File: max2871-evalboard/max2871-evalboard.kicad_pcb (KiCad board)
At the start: 4 copper layers, 50 x 80 mm, 117 parts, among them J101 USB_B_Mini, J102 Conn_02x05, J103 Conn_02x06_Odd_Even, J104 Conn_Coaxial, J105 Conn_Coaxial, Q201 2N7002, Q202 2N7002, SW101 XKBS22E05-Z, SW201 SW_Push, SW202 SW_Push, U201 AZ1117-3.3, U202 W25Q128JVS, U203 RP2040, U301 LP5907MFX-3.3, U302 LP5907MFX-3.3, U303 LP5907MFX-1.8, U304 54M_P3225, U305 MAX2871ETJ+, Y201 Crystal

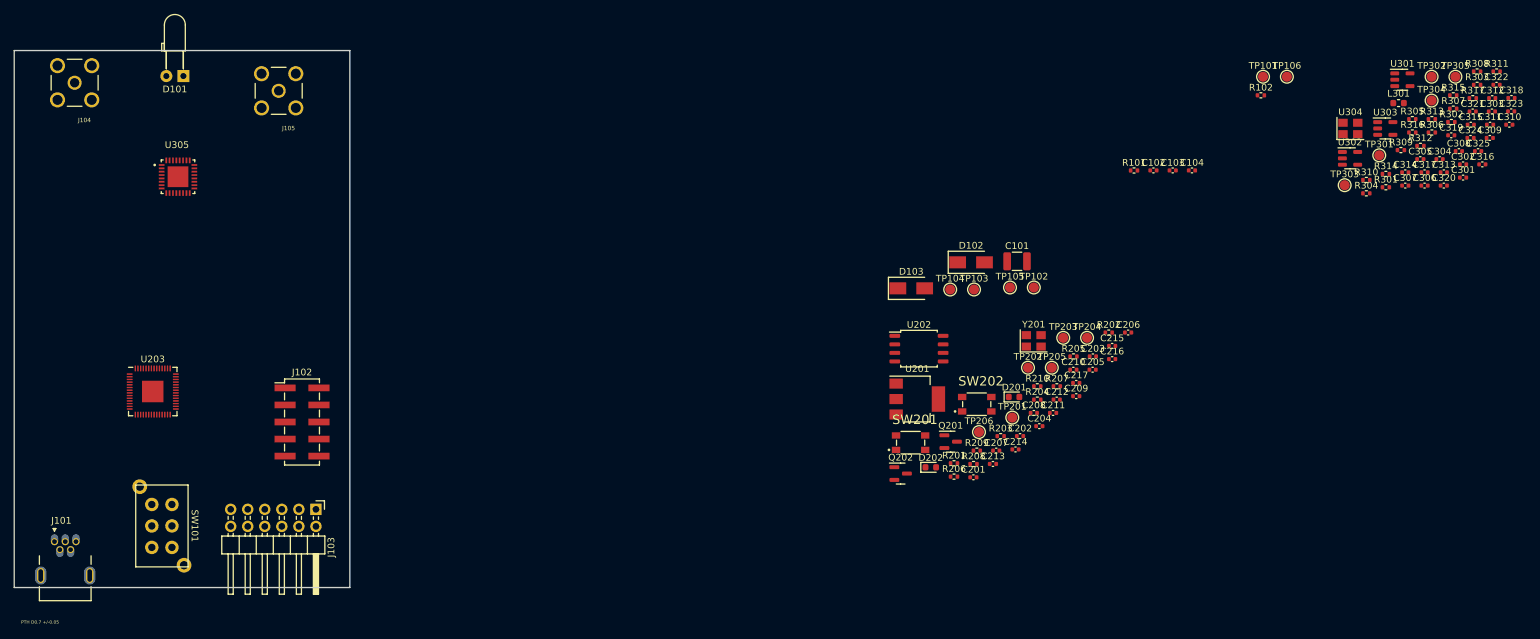
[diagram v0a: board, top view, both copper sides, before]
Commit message: Finished schematics - started PCB design
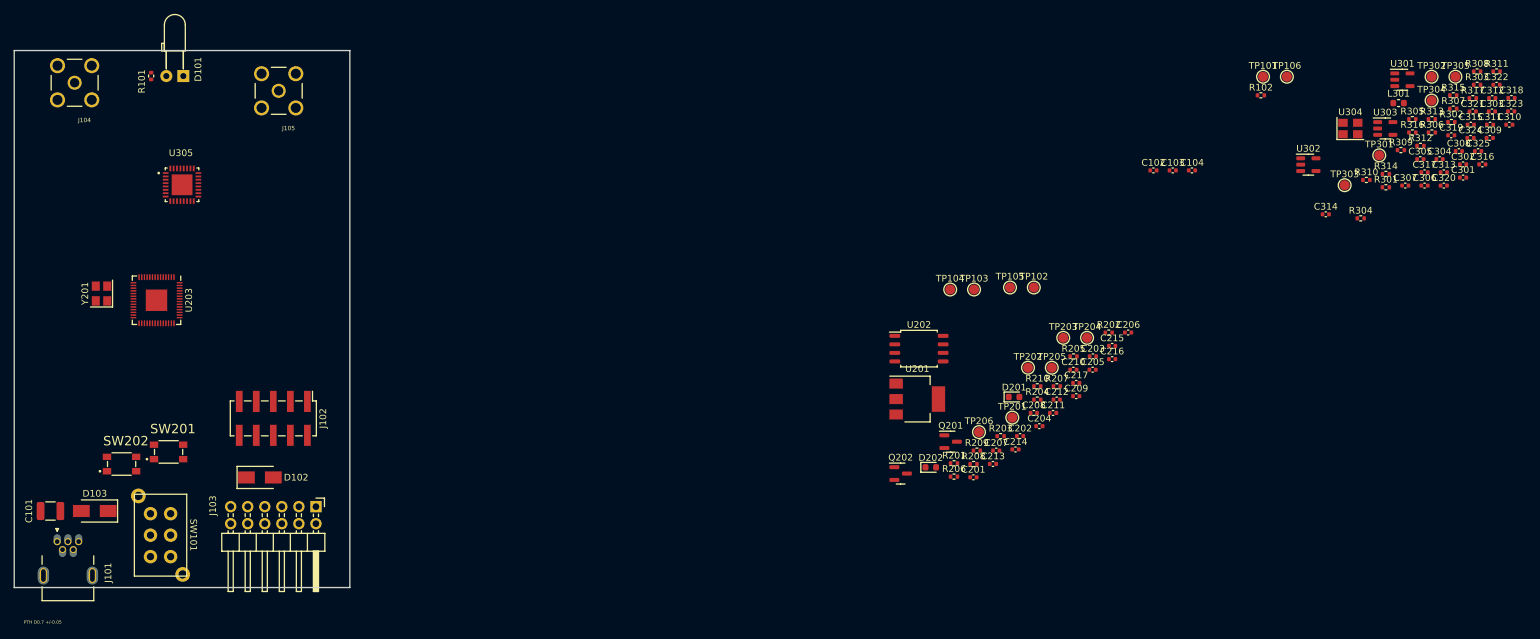
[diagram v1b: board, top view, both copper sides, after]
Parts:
- moved C101 148.7 mm to (55.4, 118.6), turned to 180 degrees
- moved R101 147.1 mm to (70.4, 53.8), turned to -90 degrees
- moved Y201 139.1 mm to (63.0, 86.2), turned to 90 degrees
- moved SW202 127.7 mm to (66.0, 111.6)
- moved D103 126.1 mm to (62.0, 118.6), turned to 180 degrees
- moved D102 110.7 mm to (86.6, 113.6)
- moved SW201 110.6 mm to (73.0, 109.8)
- moved U203 13.6 mm to (71.2, 87.2), turned to -90 degrees
- moved C314 13.4 mm to (245.4, 74.4)
- moved U302 6.28 mm to (242.8, 67.0)
- moved J102 4.31 mm to (88.6, 104.8), turned to -90 degrees
- moved R304 3.82 mm to (250.6, 75.0)
- moved SW101 1.39 mm to (71.8, 122.2)
- moved U305 1.34 mm to (75.0, 70.0)
- moved J101 0.40 mm to (56.4, 123.2)
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
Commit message: PCB placement complete
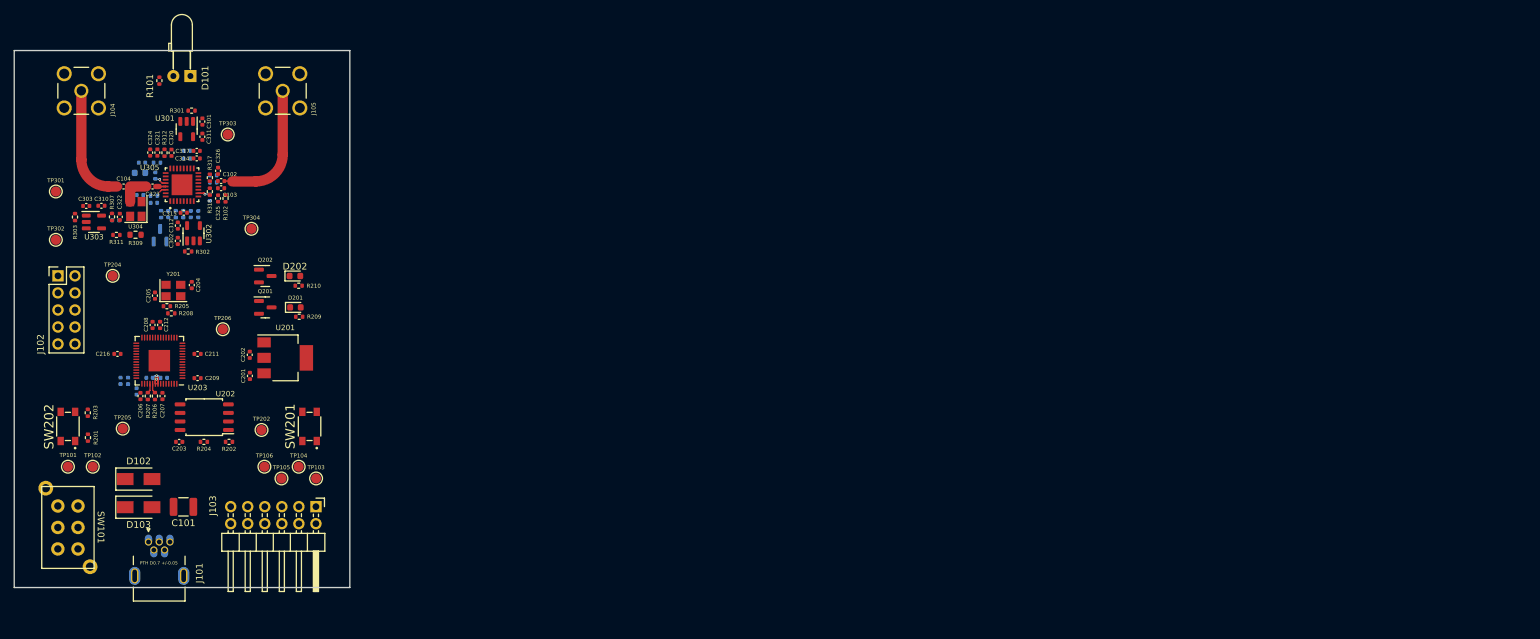
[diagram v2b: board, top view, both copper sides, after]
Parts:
- removed TP201, TP203: , TestPoint:TestPoint_Pad_D1.5mm
- removed the TP304 at (261.2, 57.5)
- added C319: 100pF, Capacitor_SMD:C_0402_1005Metric, B.Cu at (72.9, 74.4)
- added Q301: 2N7002, Package_TO_SOT_SMD:SOT-23, B.Cu at (71.7, 77.5)
- added R310: 1k, Resistor_SMD:R_0402_1005Metric, B.Cu at (71.9, 74.4)
- C210, C213, C214, C215, C217, C304, C305, C306, C307, C308, C309, C313, C316, C318, L301, R304, R305, R306, R308: moved to B.Cu
- J102: footprint Connector_PinHeader_2.54mm:PinHeader_2x05_P2.54mm_Vertical_SMD -> Connector_PinHeader_2.54mm:PinHeader_2x05_P2.54mm_Vertical
- R309: footprint Resistor_SMD:R_0402_1005Metric -> Resistor_SMD:R_0603_1608Metric
- R313: renamed from R312; moved to B.Cu
- R314: renamed from R313; moved to B.Cu
- R315: renamed from R314; moved to B.Cu
- R316: renamed from R315; moved to B.Cu
- moved C310 210.1 mm to (63.0, 73.1), turned to 180 degrees
- moved TP302 209.9 mm to (56.2, 78.2)
- moved C303 209.9 mm to (60.7, 73.2)
- moved R303 209.8 mm to (59.1, 74.8), turned to -90 degrees
- moved R308 204.0 mm to (65.1, 75.3), turned to 180 degrees
- moved C324 202.9 mm to (70.3, 65.2), turned to 90 degrees
- moved C322 202.2 mm to (65.7, 74.8), turned to -90 degrees
- moved C309 200.8 mm to (69.0, 66.7), turned to 180 degrees
- moved C323 200.8 mm to (70.6, 70.3), turned to 180 degrees
- moved R307 200.5 mm to (64.6, 74.8), turned to -90 degrees
- moved R312 198.8 mm to (72.4, 65.2), turned to 90 degrees
- moved C316 198.0 mm to (70.8, 72.7), turned to 180 degrees
- moved TP301 197.2 mm to (56.2, 71.0)
- moved C312 196.7 mm to (74.4, 76.1), turned to -90 degrees
- moved C318 194.5 mm to (79.1, 71.9), turned to -90 degrees
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- renumbered C319 to C320, C320 to C321, C321 to C322, C322 to C323, C323 to C324, C324 to C325, C325 to C326, R310 to R311, R311 to R312, R316 to R317, R317 to R318, TP305 to TP302, TP302 to TP303, TP303 to TP304
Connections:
- J103 pad 8: /CE -> /LE
- TP106 pad 1: /CE -> /LE
- U203 pad 12: /microcontroller/VCO_LE -> unconnected-(U203-Pad12)
- U203 pad 13: unconnected-(U203-Pad13) -> /microcontroller/LED1
- U203 pad 14: unconnected-(U203-Pad14) -> /microcontroller/LED2
- U203 pad 36: /microcontroller/LED1 -> unconnected-(U203-Pad36)
- U203 pad 37: /microcontroller/LED2 -> unconnected-(U203-Pad37)
- U203 pad 7: /microcontroller/VCO_MUX -> /microcontroller/VCO_CE
- U305 pad 3: /microcontroller/VCO_LE -> /LE
- U305 pad 4: /CE -> Net-(C319-Pad1)
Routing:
- net Net-(C102-Pad2): track 0.00 -> 26.8 mm
- net Net-(C104-Pad1): track 0.00 -> 23.0 mm
- net +3V3: track 0.00 -> 7.25 mm, vias 0 -> 2
- net /vco/REF_CLK: track 0.00 -> 5.11 mm
- net /vco/VCC_DIG: track 0.00 -> 2.05 mm, vias 0 -> 1
- net Net-(C323-Pad1): track 0.00 -> 1.98 mm
- net /vco/VCC_PLL: track 0.00 -> 1.78 mm, vias 0 -> 1
- net Net-(R206-Pad2): track 0.00 -> 1.46 mm
- net Net-(R207-Pad2): track 0.00 -> 1.45 mm
- net /MUX: track 0.00 -> 1.02 mm

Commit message: Finish PCB design
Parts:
- moved TP204 11.2 mm to (54.7, 78.5)
- moved TP202 8.16 mm to (80.1, 111.1)
- moved C101 6.90 mm to (68.4, 119.3), turned to 180 degrees
- moved TP302 3.57 mm to (55.5, 74.7)
- moved D103 2.51 mm to (68.5, 115.5)
- moved D102 2.16 mm to (68.5, 111.7)
- moved TP206 1.84 mm to (79.2, 91.3)
- moved TP303 1.63 mm to (80.2, 62.4)
- moved R208 1.03 mm to (74.0, 90.0)
- moved C201 1.01 mm to (85.1, 97.5), turned to 90 degrees
- moved R205 0.86 mm to (73.0, 88.9)
- moved C204 0.86 mm to (76.7, 85.8)
- moved C205 0.86 mm to (71.2, 87.3)
- moved Y201 0.86 mm to (74.0, 86.6)
- moved R302 0.76 mm to (76.7, 79.9)
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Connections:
- J101 pad 6: GND -> (no net)
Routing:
- net +3V3: track 7.25 -> 114.2 mm, vias 2 -> 23
- net /PWR: track 0.00 -> 82.4 mm, vias 0 -> 18
- net /DATA: track 0.00 -> 69.7 mm
- net /MUX: track 1.02 -> 64.4 mm, vias 0 -> 1
- net /SCLK: track 0.00 -> 62.6 mm
- net /microcontroller/VCO_LD: track 0.00 -> 61.0 mm, vias 0 -> 3
- net /EN_TXCO: track 0.00 -> 60.3 mm, vias 0 -> 1
- net /RESET: track 0.00 -> 58.1 mm, vias 0 -> 1
- net /LE: track 0.00 -> 57.3 mm, vias 0 -> 2
- net /microcontroller/VCOOUT_EN: track 0.00 -> 56.6 mm, vias 0 -> 3
- net /TXCO_PWR: track 0.00 -> 54.8 mm, vias 0 -> 1
- net GND: track 0.00 -> 51.9 mm, vias 0 -> 231
- net /SPI_CLK: track 0.00 -> 50.1 mm, vias 0 -> 1
- net /SPI_DATA: track 0.00 -> 47.0 mm, vias 0 -> 1
- net /SPI_MISO: track 0.00 -> 41.2 mm, vias 0 -> 1
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- added copper zone on F.Cu, net +3V3
- added copper zone on In1.Cu, net +3V3
- added copper zone on B.Cu, net /PWR
- added copper zone on F.Cu, net /PWR
- added copper zone on In1.Cu, net /PWR
- added copper zone on B.Cu, net GND
- added copper zone on F.Cu, net GND
- added copper zone on In1.Cu, net GND
- added copper zone on In2.Cu, net GND

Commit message: Finish layout design
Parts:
- removed the C302 at (74.4, 78.4)
- removed the C303 at (60.7, 73.2)
- removed the C310 at (63.0, 73.1)
- removed the C312 at (74.4, 76.1)
- removed the R302 at (76.7, 79.9)
- removed the R303 at (59.1, 74.8)
- removed the R308 at (65.1, 75.3)
- removed the TP302 at (55.5, 74.7)
- removed the U302 at (76.7, 77.2)
- removed the U303 at (61.9, 75.5)
- added C204: 2.2uF, Capacitor_SMD:C_0402_1005Metric, F.Cu at (72.9, 106.6)
- added C304: 100nF, Capacitor_SMD:C_0402_1005Metric, F.Cu at (77.2, 63.0)
- added C305: 100nF, Capacitor_SMD:C_0402_1005Metric, F.Cu at (78.2, 74.7)
- added C315: 100pF, Capacitor_SMD:C_0402_1005Metric, F.Cu at (78.8, 66.3)
- added C316: 100pF, Capacitor_SMD:C_0402_1005Metric, F.Cu at (75.2, 74.0)
- added D201: LED, LED_THT:LED_D3.0mm_Horizontal_O3.81mm_Z2.0mm, F.Cu at (81.5, 53.7)
- added L301: BLM18PG181S, Inductor_SMD:L_0603_1608Metric, F.Cu at (76.6, 61.5)
- added L302: BLM18PG181S, Inductor_SMD:L_0603_1608Metric, F.Cu at (81.5, 75.9)
- added Q201: 2N7002, Package_TO_SOT_SMD:SOT-23, F.Cu at (80.3, 58.2)
- added R101: DNP, Resistor_SMD:R_0402_1005Metric, F.Cu at (68.2, 120.4)
- added R102: 5.1k, Resistor_SMD:R_0402_1005Metric, F.Cu at (75.3, 119.6)
- added R103: DNP, Resistor_SMD:R_0402_1005Metric, F.Cu at (67.1, 120.4)
- added R104: 5.1k, Resistor_SMD:R_0402_1005Metric, F.Cu at (74.1, 119.6)
- added R209: 1k, Resistor_SMD:R_0402_1005Metric, F.Cu at (79.3, 55.6)
- added REF**: MountingHole_2.7mm_M2.5_DIN965, MountingHole:MountingHole_2.7mm_M2.5_DIN965, F.Cu at (96.0, 65.0)
- added REF**: MountingHole_2.7mm_M2.5_DIN965, MountingHole:MountingHole_2.7mm_M2.5_DIN965, F.Cu at (54.0, 110.0)
- added REF**: MountingHole_2.7mm_M2.5_DIN965, MountingHole:MountingHole_2.7mm_M2.5_DIN965, F.Cu at (96.0, 110.0)
- added REF**: MountingHole_2.7mm_M2.5_DIN965, MountingHole:MountingHole_2.7mm_M2.5_DIN965, F.Cu at (54.0, 65.0)
- added REF**: OSHW-Logo2_14.6x12mm_SilkScreen, Symbol:OSHW-Logo2_14.6x12mm_SilkScreen, B.Cu at (64.8, 105.2)
- C101: value 47uF -> 10uF; footprint Capacitor_SMD:C_1210_3225Metric -> Capacitor_SMD:C_0603_1608Metric
- C201: value 1uF -> 10uF; footprint Capacitor_SMD:C_0402_1005Metric -> Capacitor_SMD:C_0603_1608Metric
- C202: value 1uF -> 22uF; footprint Capacitor_SMD:C_0402_1005Metric -> Capacitor_SMD:C_0805_2012Metric
- J101: value USB_B_Mini -> USB_C_Receptacle_USB2.0; footprint 54819-0519:MOLEX_54819-0519 -> USB4105-GF-A:GCT_USB4105-GF-A
- J103: renamed from J102; footprint Connector_PinHeader_2.54mm:PinHeader_2x05_P2.54mm_Vertical -> Connector_PinHeader_1.27mm:PinHeader_2x05_P1.27mm_Vertical
- TP101: renamed from TP103; footprint TestPoint:TestPoint_Pad_D1.5mm -> TestPoint:TestPoint_Pad_D1.0mm
- TP102: renamed from TP104; footprint TestPoint:TestPoint_Pad_D1.5mm -> TestPoint:TestPoint_Pad_D1.0mm
- TP103: renamed from TP105; footprint TestPoint:TestPoint_Pad_D1.5mm -> TestPoint:TestPoint_Pad_D1.0mm
- TP104: renamed from TP106; footprint TestPoint:TestPoint_Pad_D1.5mm -> TestPoint:TestPoint_Pad_D1.0mm
- moved R301 21.8 mm to (80.8, 80.3)
- moved C301 19.4 mm to (75.6, 79.9), turned to 90 degrees
- moved U301 17.2 mm to (77.9, 78.7), turned to 90 degrees
- moved C317 15.0 mm to (75.6, 77.6), turned to -90 degrees
- moved TP301 7.92 mm to (73.7, 57.9)
- moved D103 4.75 mm to (71.5, 53.8)
- moved J101 4.48 mm to (72.1, 127.2)
- moved SW201 2.50 mm to (91.5, 106.0)
- moved R203 2.21 mm to (59.6, 102.2), turned to 0 degrees
- moved R105 1.80 mm to (70.4, 55.8), turned to 0 degrees
- moved J103 1.78 mm to (56.9, 85.3)
- moved TP302 1.47 mm to (84.5, 75.3)
- moved C306 1.37 mm to (77.2, 64.7)
- moved TP101 1.33 mm to (93.7, 114.2)
- moved R201 1.20 mm to (61.6, 108.7), turned to 90 degrees
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- renumbered C204 to C205, C205 to C206, C206 to C207, C207 to C208, C208 to C209, C209 to C210, C210 to C211, C211 to C212, C212 to C213, C213 to C214, C214 to C215, C215 to C216, C216 to C217, C217 to C218, C304 to C302, C305 to C303, C314 to C306, C315 to C307, C306 to C308, C307 to C309, C308 to C310, C309 to C311, C317 to C312, C318 to C313, C313 to C314, C311 to C317, C316 to C318, D102 to D101, D103 to D102, D101 to D103, D201 to D202, D202 to D203, J103 to J102, L301 to L303, Q201 to Q202, Q202 to Q203, R101 to R105, R102 to R106, R209 to R210, R210 to R211, R304 to R302, R307 to R303, R305 to R304, R306 to R305, R309 to R306, R310 to R307, R311 to R308, R312 to R309, R313 to R310, R314 to R311, R315 to R312, R316 to R313, R317 to R314, R318 to R315, TP102 to TP105, TP101 to TP106, TP202 to TP201, TP204 to TP202, TP205 to TP203, TP206 to TP204, TP303 to TP301, TP304 to TP302, TP301 to TP303, U304 to U302, U305 to U303
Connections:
- C101 pad 1: Net-(C101-Pad1) -> /VBUS
- C317 pad 1: /vco/VCC_VCO -> Net-(C317-Pad1)
- D102 pad 2: Net-(C101-Pad1) -> /VBUS
- J103 pad 3: /SWD -> /SWCLK
- J103 pad 4: /SWCLK -> /SWD
- R303 pad 1: Net-(C310-Pad1) -> /vco/VCC_DIG
- U203 pad 36: unconnected-(U203-Pad36) -> /microcontroller/LED_LOCK
- U301 pad 5: /vco/VCC_VCO -> Net-(C317-Pad1)
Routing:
- net /PWR: track 82.4 -> 9.32 mm, vias 18 -> 16
- net /microcontroller/LED_LOCK: track 0.00 -> 68.4 mm, vias 0 -> 2
- net Net-(C317-Pad1): track 0.00 -> 40.0 mm, vias 0 -> 4
- net GND: track 51.9 -> 77.8 mm, vias 231 -> 274
- net Net-(J101-PadA5): track 0.00 -> 17.9 mm, vias 0 -> 3
- net /vco/VCC_TXCO: track 19.9 -> 7.36 mm, vias 1 -> 0
- net Net-(C102-Pad2): track 26.8 -> 14.2 mm
- net +3V3: track 114.2 -> 124.8 mm, vias 23 -> 25
- net Net-(C104-Pad1): track 23.0 -> 12.6 mm
- net Net-(C101-Pad1): track 10.1 -> 0.00 mm, vias 1 -> 0
- net Net-(J101-PadB5): track 0.00 -> 9.22 mm, vias 0 -> 2
- net /SWCLK: track 14.9 -> 23.1 mm
- net /VBUS: track 0.00 -> 6.48 mm, vias 0 -> 2
- net /vco/VCC_VCO: track 26.0 -> 30.7 mm, vias 5 -> 3
- net Net-(D201-Pad1): track 0.00 -> 4.61 mm
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- added copper zone on In2.Cu, net +3V3
- added copper zone on F.Cu, net /VBUS
- removed copper zone on In1.Cu, net +3V3
- removed copper zone on In1.Cu, net /PWR
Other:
- board text added: "Copyright (C) 2023 The Antenna Guy"
- board text added: "JLCJLCJLCJLC"
- board text added: "MAX2871 Synthetizer Evaluation Board"

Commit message: Finish PCB - generate fabrication files
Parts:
- moved REF** 21.7 mm to (86.5, 105.0)
- moved D101 0.70 mm to (67.8, 111.7)
- moved D102 0.70 mm to (67.8, 115.5)
- renumbered SW201 to BOOT, SW202 to RESET
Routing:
- net /PWR: track 9.32 -> 52.0 mm, vias 16 -> 12
- net Net-(D101-Pad2): track 32.4 -> 30.6 mm
- net +5V: track 22.3 -> 20.9 mm
- net GND: track 77.8 -> 78.5 mm, vias 274 -> 290
- net +3V3: track 124.8 -> 125.3 mm
- net (no net): vias 1 -> 0
